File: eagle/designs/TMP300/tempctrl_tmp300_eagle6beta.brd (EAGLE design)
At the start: 64 x 48 mm, 27 parts, among them IC1 TMP300, Q1 NIF5002

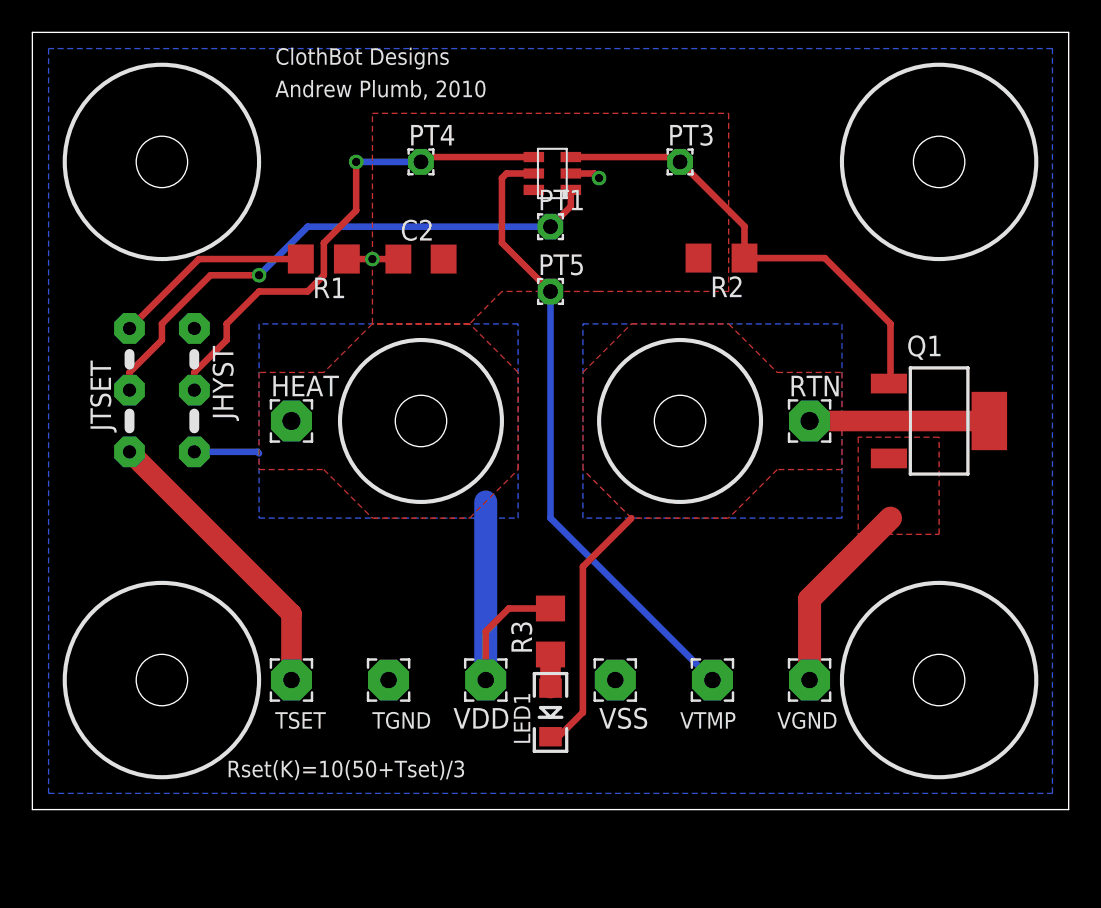
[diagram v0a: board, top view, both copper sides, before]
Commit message: Automatically modified board after jumper added and wired up on schematic side.
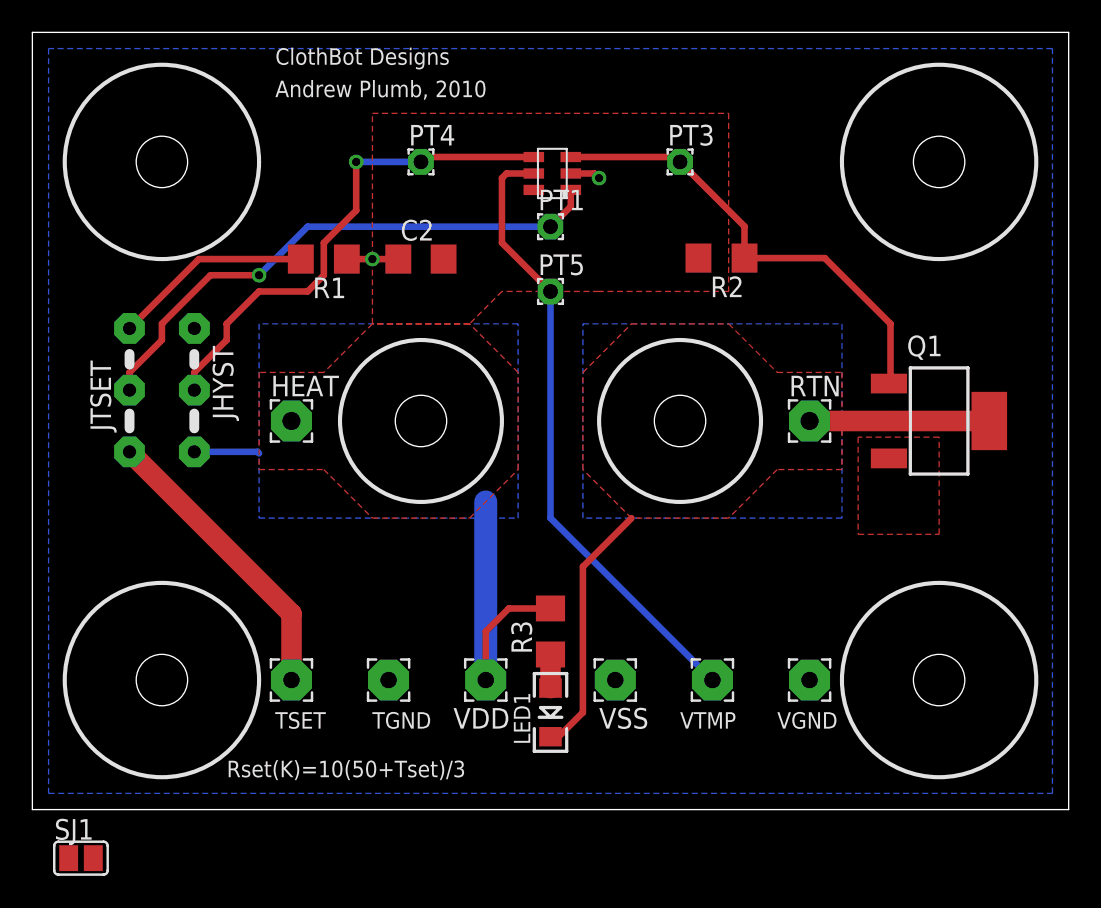
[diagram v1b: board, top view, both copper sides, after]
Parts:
- added SJ1: (no value), jumper:SJ
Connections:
- new net N$1: SJ1.1, VGND.1
- net GND: now also SJ1.2; no longer VGND.1
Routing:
- net GND: track 17.1 -> 5.04 mm
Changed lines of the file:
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@@
 <element name="U$5" library="special-drill" package="DRILL_0.1250" value="" x="24" y="24"/>
 <element name="U$6" library="special-drill" package="DRILL_0.1250" value="" x="40" y="24"/>
+<element name="SJ1" library="jumper" package="SJ" value="" x="3" y="-3"/>
 </elements>
 <signals>
 <signal name="GND">
 <contactref element="R1" pad="1"/>
-<contactref element="VGND" pad="1"/>
 <contactref element="IC1" pad="2"/>
 <contactref element="TGND" pad="1"/>
@@
 <contactref element="Q1" pad="3"/>
 <contactref element="VSS" pad="1"/>
-<wire x1="48" y1="8" x2="48" y2="13" width="1.4224" layer="1"/>
-<wire x1="48" y1="13" x2="53" y2="18" width="1.4224" layer="1"/>
 <wire x1="33.254" y1="39.286" x2="34.714" y2="39.286" width="0.4064" layer="1"/>
 <wire x1="34.714" y1="39.286" x2="35" y2="39" width="0.4064" layer="1"/>
@@
 <vertex x="56" y="23"/>
 </polygon>
+<contactref element="SJ1" pad="2"/>
+<wire x1="36" y1="8" x2="52.901" y2="21.689" width="0" layer="19" extent="1-1"/>
+<wire x1="22" y1="8" x2="36" y2="8" width="0" layer="19" extent="1-1"/>
+<wire x1="3.762" y1="-3" x2="22" y2="8" width="0" layer="19" extent="1-1"/>
+<wire x1="10" y1="29.715" x2="22" y2="8" width="0" layer="19" extent="1-1"/>
+<wire x1="19.422" y1="34" x2="10" y2="29.715" width="0" layer="19" extent="1-1"/>
+<wire x1="33.254" y1="39.286" x2="22.6" y2="34" width="0" layer="19" extent="1-1"/>
 </signal>
 <signal name="N$4">
@@
 <wire x1="53" y1="24" x2="59" y2="24" width="1.27" layer="1"/>
 </signal>
+<signal name="N$1">
+<contactref element="VGND" pad="1"/>
+<contactref element="SJ1" pad="1"/>
+<wire x1="2.238" y1="-3" x2="48" y2="8" width="0" layer="19" extent="1-1"/>
+</signal>
 </signals>

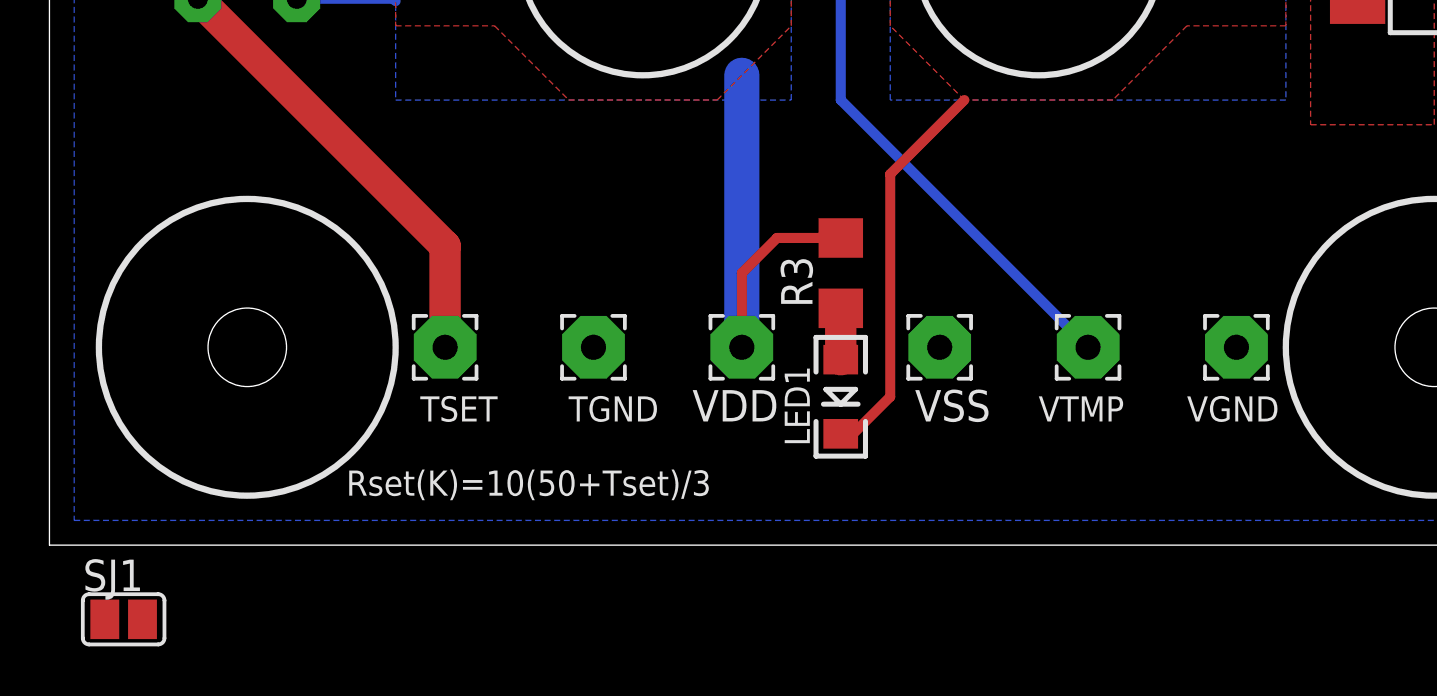
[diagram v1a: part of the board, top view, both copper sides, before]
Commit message: Moved jumper near final position; rotate part seems broken.
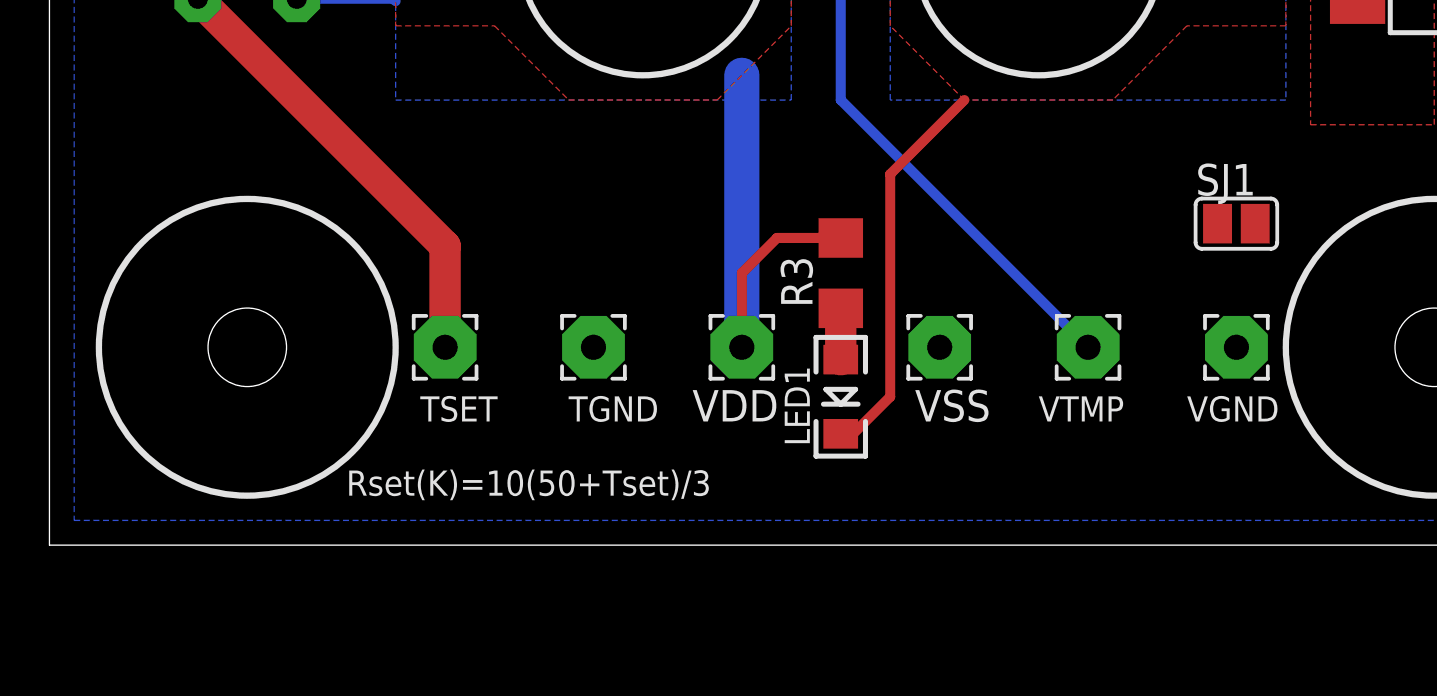
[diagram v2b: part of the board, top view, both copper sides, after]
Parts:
- moved SJ1 47.8 mm to (48.0, 13.0)
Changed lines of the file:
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@@
 <element name="U$5" library="special-drill" package="DRILL_0.1250" value="" x="24" y="24"/>
 <element name="U$6" library="special-drill" package="DRILL_0.1250" value="" x="40" y="24"/>
-<element name="SJ1" library="jumper" package="SJ" value="" x="3" y="-3"/>
+<element name="SJ1" library="jumper" package="SJ" value="" x="48" y="13"/>
 </elements>
 <signals>
@@
 <wire x1="36" y1="8" x2="52.901" y2="21.689" width="0" layer="19" extent="1-1"/>
 <wire x1="22" y1="8" x2="36" y2="8" width="0" layer="19" extent="1-1"/>
-<wire x1="3.762" y1="-3" x2="22" y2="8" width="0" layer="19" extent="1-1"/>
+<wire x1="48.762" y1="13" x2="22" y2="8" width="0" layer="19" extent="1-1"/>
 <wire x1="10" y1="29.715" x2="22" y2="8" width="0" layer="19" extent="1-1"/>
 <wire x1="19.422" y1="34" x2="10" y2="29.715" width="0" layer="19" extent="1-1"/>
@@
 <contactref element="VGND" pad="1"/>
 <contactref element="SJ1" pad="1"/>
-<wire x1="2.238" y1="-3" x2="48" y2="8" width="0" layer="19" extent="1-1"/>
+<wire x1="47.238" y1="13" x2="48" y2="8" width="0" layer="19" extent="1-1"/>
 </signal>
 </signals>
